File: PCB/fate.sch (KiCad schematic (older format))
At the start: 33 parts, among them J1 XLR3, J10 Conn_01x01, J2 Conn_Coaxial, J3 Conn_Coaxial, J4 Conn_Coaxial, J5 Conn_Coaxial, J6 XLR3, J7 Conn_01x01, J8 Conn_01x01, J9 Conn_01x01

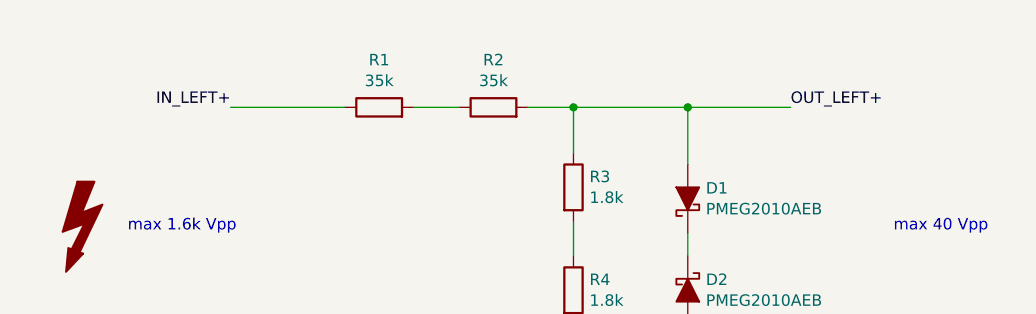
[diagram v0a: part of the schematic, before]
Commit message: Update resistors to use "NS" resistors
"NS" resistors have a special winding to be "non-inductive".
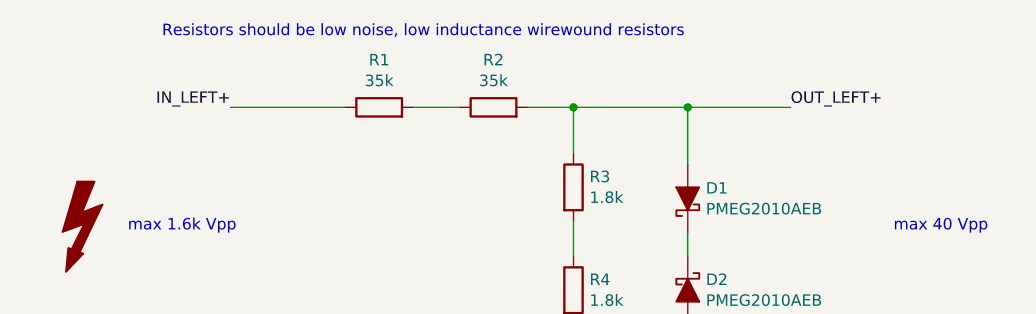
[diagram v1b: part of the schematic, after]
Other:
- note added: "Resistors should be low noise, low inductance wirewound resistors"
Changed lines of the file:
@@
 F 1 "1.8k" H 3670 1305 50  0000 L CNN
 F 2 "Resistor_THT:R_Axial_DIN0516_L15.5mm_D5.0mm_P25.40mm_Horizontal" V 3530 1350 50  0001 C CNN
-F 3 "https://www.mouser.de/ProductDetail/Vishay-Dale/RS02B1K800FE12?qs=sGAEpiMZZMtbXrIkmrvidDnVsdYYat5o0IDxxm9WPSA%3d" H 3600 1350 50  0001 C CNN
+F 3 "https://www.mouser.de/ProductDetail/Vishay-Dale/NS02B1K800FE12?qs=sGAEpiMZZMtbXrIkmrvidDdY%2fwKIbxTCkkyAtkN081w%3d" H 3600 1350 50  0001 C CNN
 	1    3600 1350
 	1    0    0    -1
@@
 F 1 "1.8k" H 3620 3005 50  0000 L CNN
 F 2 "Resistor_THT:R_Axial_DIN0516_L15.5mm_D5.0mm_P25.40mm_Horizontal" V 3480 3050 50  0001 C CNN
-F 3 "https://www.mouser.de/ProductDetail/Vishay-Dale/RS02B1K800FE12?qs=sGAEpiMZZMtbXrIkmrvidDnVsdYYat5o0IDxxm9WPSA%3d" H 3550 3050 50  0001 C CNN
+F 3 "https://www.mouser.de/ProductDetail/Vishay-Dale/NS02B1K800FE12?qs=sGAEpiMZZMtbXrIkmrvidDdY%2fwKIbxTCkkyAtkN081w%3d" H 3550 3050 50  0001 C CNN
 	1    3550 3050
 	1    0    0    -1
@@
 F 1 "1.8k" H 3620 3455 50  0000 L CNN
 F 2 "Resistor_THT:R_Axial_DIN0516_L15.5mm_D5.0mm_P25.40mm_Horizontal" V 3480 3500 50  0001 C CNN
-F 3 "https://www.mouser.de/ProductDetail/Vishay-Dale/RS02B1K800FE12?qs=sGAEpiMZZMtbXrIkmrvidDnVsdYYat5o0IDxxm9WPSA%3d" H 3550 3500 50  0001 C CNN
+F 3 "https://www.mouser.de/ProductDetail/Vishay-Dale/NS02B1K800FE12?qs=sGAEpiMZZMtbXrIkmrvidDdY%2fwKIbxTCkkyAtkN081w%3d" H 3550 3500 50  0001 C CNN
 	1    3550 3500
 	1    0    0    -1
@@
 F 1 "1.8k" H 3670 1755 50  0000 L CNN
 F 2 "Resistor_THT:R_Axial_DIN0516_L15.5mm_D5.0mm_P25.40mm_Horizontal" V 3530 1800 50  0001 C CNN
-F 3 "https://www.mouser.de/ProductDetail/Vishay-Dale/RS02B1K800FE12?qs=sGAEpiMZZMtbXrIkmrvidDnVsdYYat5o0IDxxm9WPSA%3d" H 3600 1800 50  0001 C CNN
+F 3 "https://www.mouser.de/ProductDetail/Vishay-Dale/NS02B1K800FE12?qs=sGAEpiMZZMtbXrIkmrvidDdY%2fwKIbxTCkkyAtkN081w%3d" H 3600 1800 50  0001 C CNN
 	1    3600 1800
 	1    0    0    -1
@@
 	1    0    0    -1
 $EndComp
+Text Notes 1800 700  0    50   ~ 0
+Resistors should be low noise, low inductance wirewound resistors
 $EndSCHEMATC

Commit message: Add ground reference between differential signal lines
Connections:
- net GND: now also R10.1, R3.2, R4.1, R9.2
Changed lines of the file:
@@
 Connection ~ 3600 2200
 Wire Wire Line
-	3600 1650 3600 1500
+	3600 1650 3600 1600
 Wire Wire Line
 	3600 1200 3600 1000
@@
 Connection ~ 3550 3900
 Wire Wire Line
-	3550 3350 3550 3200
+	3550 3350 3550 3300
 Wire Wire Line
 	3550 2900 3550 2700
@@
 Text Notes 1800 700  0    50   ~ 0
 Resistors should be low noise, low inductance wirewound resistors
+$Comp
+L power:GND #PWR?
+U 1 1 5C5EC0A4
+P 3600 1600
+F 0 "#PWR?" H 3600 1350 50  0001 C CNN
+F 1 "GND" H 3605 1427 50  0000 C CNN
+F 2 "" H 3600 1600 50  0001 C CNN
+F 3 "" H 3600 1600 50  0001 C CNN
+	1    3600 1600
+	0    1    1    0
+$EndComp
+Connection ~ 3600 1600
+Wire Wire Line
+	3600 1600 3600 1500
+$Comp
+L power:GND #PWR?
+U 1 1 5C5ECD9E
+P 3550 3300
+F 0 "#PWR?" H 3550 3050 50  0001 C CNN
+F 1 "GND" H 3555 3127 50  0000 C CNN
+F 2 "" H 3550 3300 50  0001 C CNN
+F 3 "" H 3550 3300 50  0001 C CNN
+	1    3550 3300
+	0    1    1    0
+$EndComp
+Connection ~ 3550 3300
+Wire Wire Line
+	3550 3300 3550 3200
 $EndSCHEMATC
